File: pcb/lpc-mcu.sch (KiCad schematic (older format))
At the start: 1 part

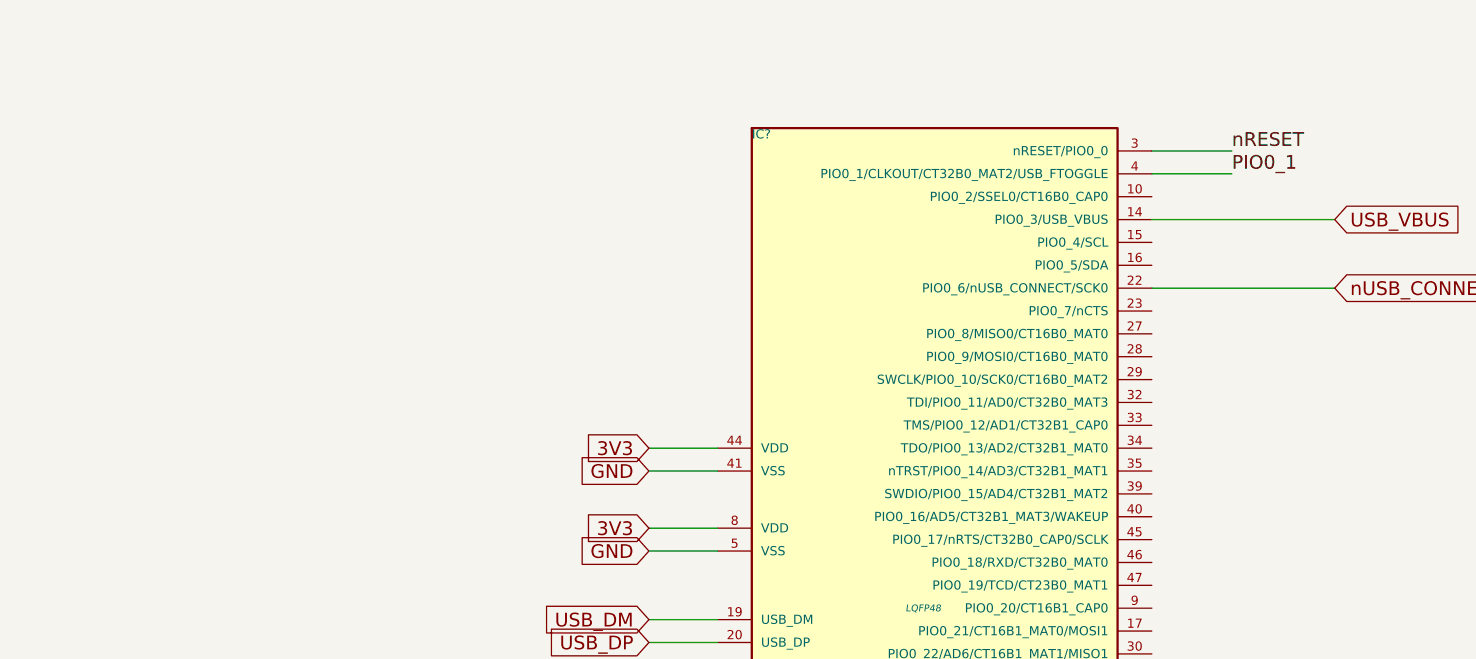
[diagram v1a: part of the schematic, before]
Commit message: added SWD connector
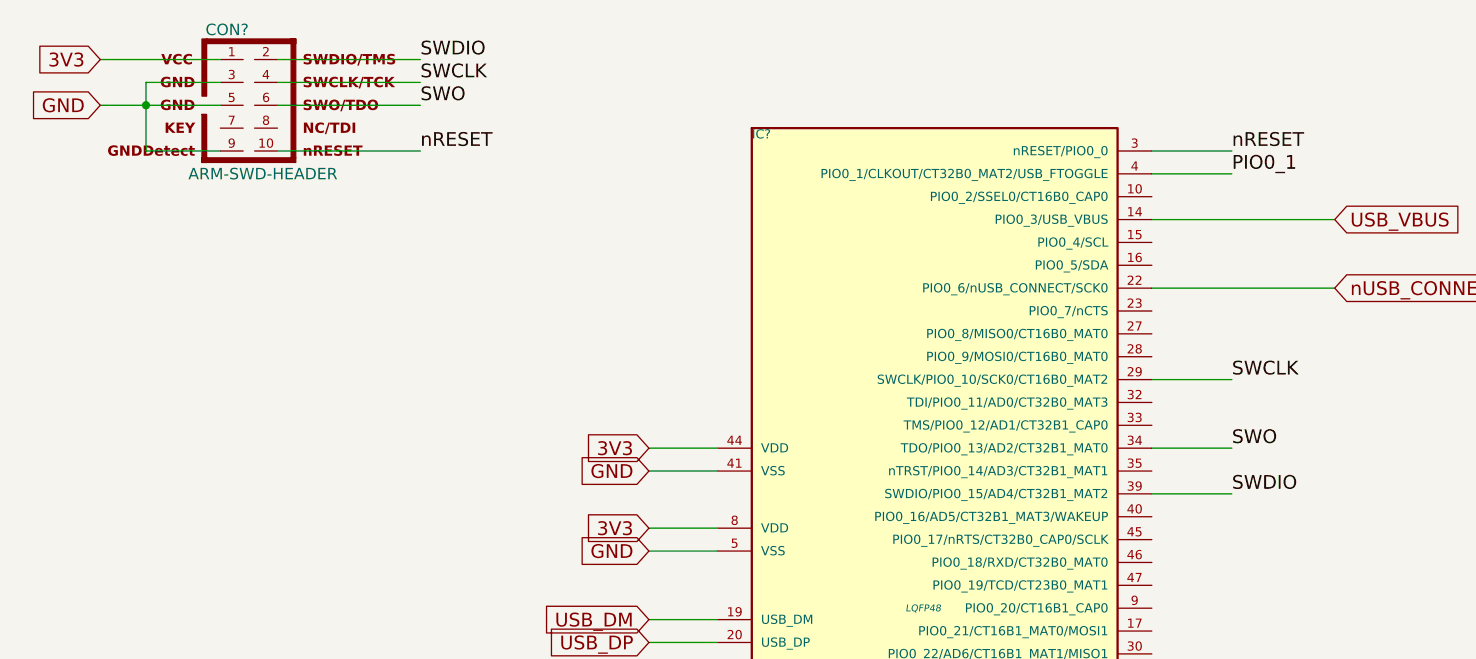
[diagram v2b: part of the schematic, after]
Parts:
- added CON?: ARM-SWD-HEADER, pin_array_5x2_50mil_smd, symbol ARM-SWD-HEADER
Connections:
- net 3V3: now also CON?.1
- net GND: now also CON?.3, CON?.5, CON?.9
- net nRESET: now also CON?.10
- net SWCLK: now reaches IC?.29 (SWCLK/PIO0_10/SCK0/CT16B0_MAT2)
- net SWCLK: now also CON?.4
- net SWO: now reaches IC?.34 (TDO/PIO0_13/AD2/CT32B1_MAT0)
- net SWO: now also CON?.6
- net SWDIO: now reaches IC?.39 (SWDIO/PIO0_15/AD4/CT32B1_MAT2)
- net SWDIO: now also CON?.2
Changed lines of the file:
@@
 Wire Wire Line
 	4350 4350 4050 4350
+$Comp
+L ARM-SWD-HEADER CON?
+U 1 1 549D5A39
+P 2300 2000
+F 0 "CON?" H 2205 2330 50  0000 C CNN
+F 1 "ARM-SWD-HEADER" H 2035 1670 50  0000 L BNN
+F 2 "pin_array_5x2_50mil_smd" V 1875 2000 50  0001 C CNN
+F 3 "~" H 2375 2000 60  0000 C CNN
+	1    2300 2000
+	1    0    0    -1
+$EndComp
+Text GLabel 1650 1800 0    60   Input ~ 0
+3V3
+Text GLabel 1650 2000 0    60   Input ~ 0
+GND
+Text Label 3050 1800 0    60   ~ 0
+SWDIO
+Text Label 3050 1900 0    60   ~ 0
+SWCLK
+Text Label 3050 2200 0    60   ~ 0
+nRESET
+Wire Wire Line
+	3050 2200 2425 2200
+Wire Wire Line
+	2425 1900 3050 1900
+Wire Wire Line
+	3050 1800 2425 1800
+Wire Wire Line
+	2175 1800 1650 1800
+Wire Wire Line
+	1650 2000 2175 2000
+Wire Wire Line
+	2175 1900 1850 1900
+Wire Wire Line
+	1850 1900 1850 2200
+Connection ~ 1850 2000
+Wire Wire Line
+	1850 2200 2175 2200
+Text Label 6600 3200 0    60   ~ 0
+SWCLK
+Text Label 6600 3700 0    60   ~ 0
+SWDIO
+Wire Wire Line
+	6600 3700 6250 3700
+Wire Wire Line
+	6250 3200 6600 3200
+Text Label 3050 2000 0    60   ~ 0
+SWO
+Text Label 6600 3500 0    60   ~ 0
+SWO
+Wire Wire Line
+	6600 3500 6250 3500
+Wire Wire Line
+	3050 2000 2425 2000
 $EndSCHEMATC

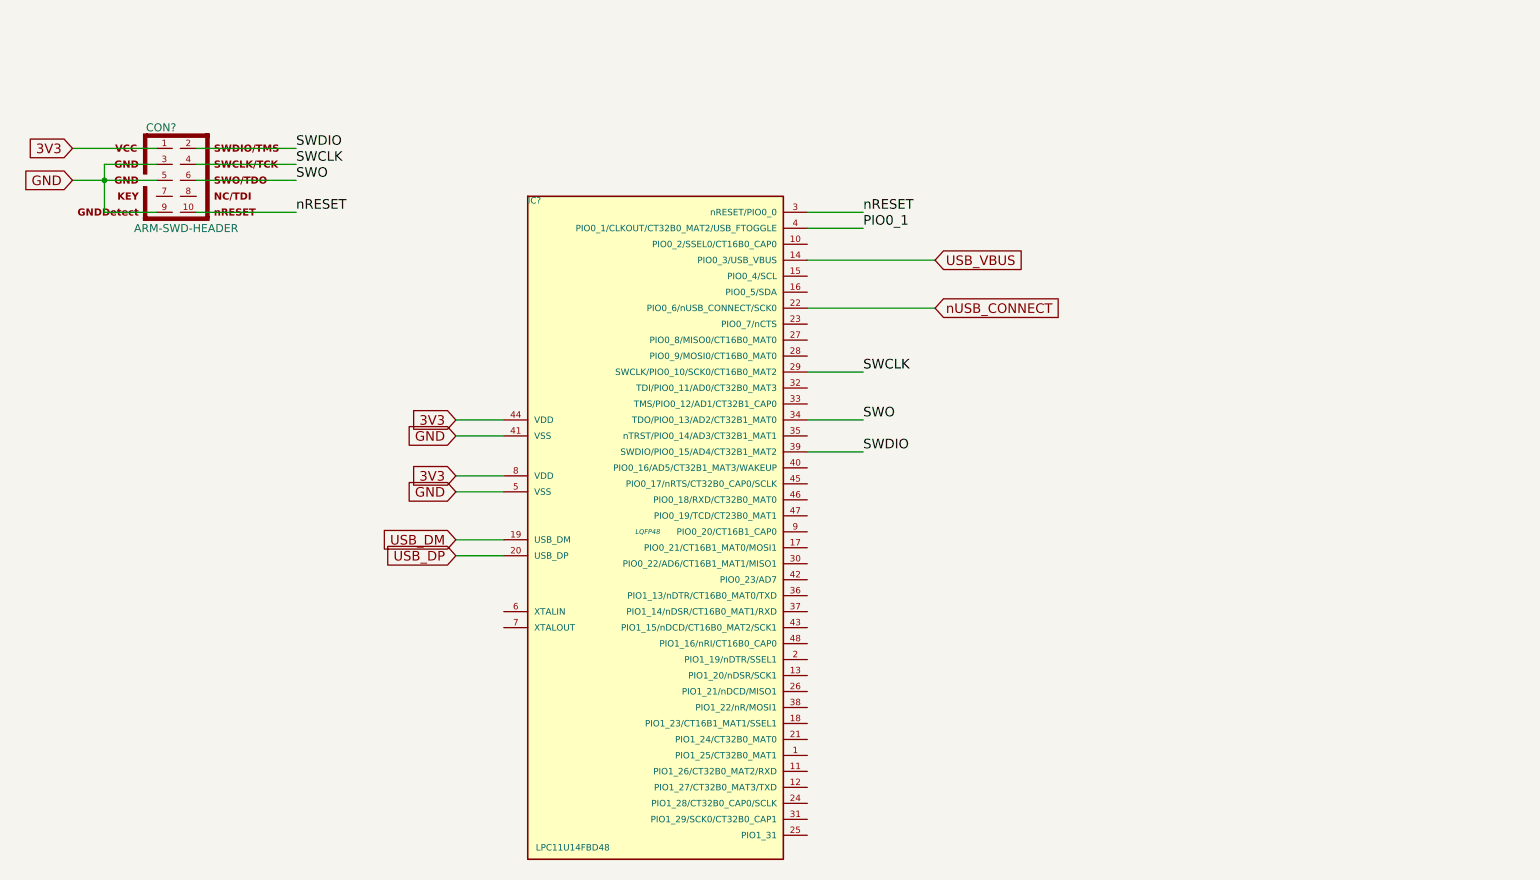
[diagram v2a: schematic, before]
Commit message: added reset pullup, some caps, usb resistors, explanation for nUSB_CONNECT
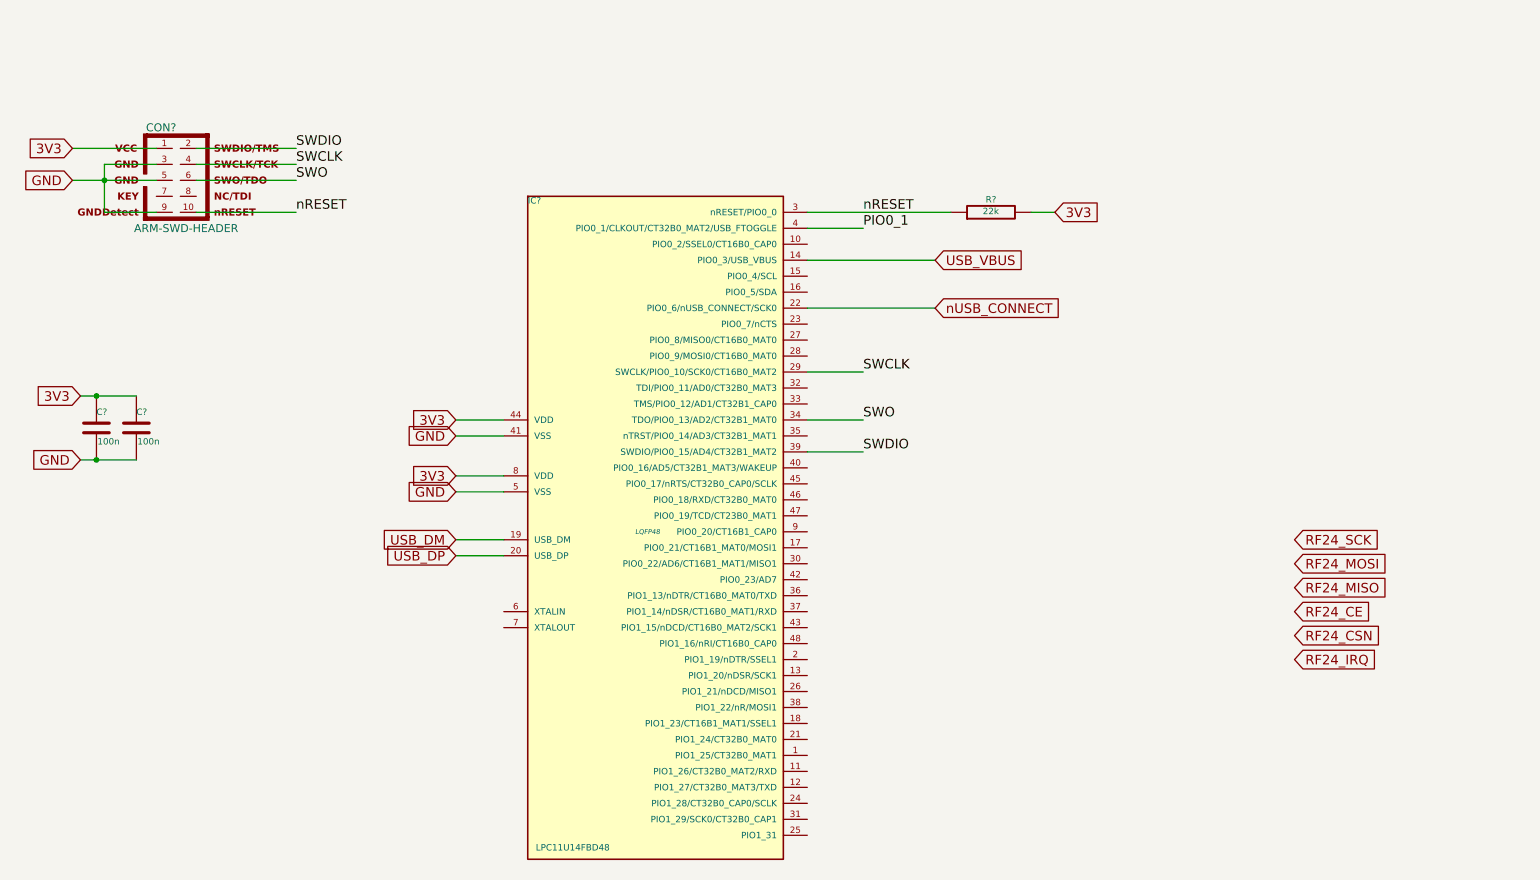
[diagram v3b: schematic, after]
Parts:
- added C? (x2): 100n, ~, symbol C
- added R?: 22k, ~, symbol R
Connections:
- net 3V3: now also C?.1, C?.1, R?.2
- net GND: now also C?.2, C?.2
- net nRESET: now also R?.1
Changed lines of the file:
@@
 	6600 2300 6250 2300
-Wire Wire Line
-	6250 2200 6600 2200
 Wire Wire Line
 	7050 2500 6250 2500
@@
 Wire Wire Line
 	3050 2000 2425 2000
+Text GLabel 9300 4250 2    60   Input ~ 0
+RF24_SCK
+Text GLabel 9300 4400 2    60   Input ~ 0
+RF24_MOSI
+Text GLabel 9300 4550 2    60   Input ~ 0
+RF24_MISO
+Text GLabel 9300 4700 2    60   Input ~ 0
+RF24_CE
+Text GLabel 9300 4850 2    60   Input ~ 0
+RF24_CSN
+Text GLabel 9300 5000 2    60   Input ~ 0
+RF24_IRQ
+$Comp
+L C C?
+U 1 1 549D5E39
+P 1800 3550
+F 0 "C?" H 1800 3650 40  0000 L CNN
+F 1 "100n" H 1806 3465 40  0000 L CNN
+F 2 "~" H 1838 3400 30  0000 C CNN
+F 3 "~" H 1800 3550 60  0000 C CNN
+	1    1800 3550
+	1    0    0    -1
+$EndComp
+$Comp
+L C C?
+U 1 1 549D5E52
+P 2050 3550
+F 0 "C?" H 2050 3650 40  0000 L CNN
+F 1 "100n" H 2056 3465 40  0000 L CNN
+F 2 "~" H 2088 3400 30  0000 C CNN
+F 3 "~" H 2050 3550 60  0000 C CNN
+	1    2050 3550
+	1    0    0    -1
+$EndComp
+Wire Wire Line
+	1700 3350 2050 3350
+Wire Wire Line
+	1700 3750 2050 3750
+Text GLabel 1700 3350 0    60   Input ~ 0
+3V3
+Text GLabel 1700 3750 0    60   Input ~ 0
+GND
+Connection ~ 1800 3750
+Connection ~ 1800 3350
+$Comp
+L R R?
+U 1 1 549D5EC0
+P 7400 2200
+F 0 "R?" V 7480 2200 40  0000 C CNN
+F 1 "22k" V 7407 2201 40  0000 C CNN
+F 2 "~" V 7330 2200 30  0000 C CNN
+F 3 "~" H 7400 2200 30  0000 C CNN
+	1    7400 2200
+	0    -1   -1   0
+$EndComp
+Text GLabel 7800 2200 2    60   Input ~ 0
+3V3
+Wire Wire Line
+	6250 2200 7150 2200
+Wire Wire Line
+	7650 2200 7800 2200
 $EndSCHEMATC

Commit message: thought through power situation a bit more, added some TO DO messages
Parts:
- added R?: NC, ~, symbol R
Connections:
- net 3V3: now also R?.1; no longer CON?.1
- new net: CON?.1, R?.2
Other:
- note added: "Debugger not connected to 3V3 by\ndefault, to avoid accidentally\nbackfeeding power into the regulator."
- note added: "One bypass cap for each VDD/VSS pair."
- note added: "TO DO: figure out if we need to reduce the USB\nbus voltage before it gets to the MCU."
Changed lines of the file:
@@
 	1    0    0    -1
 $EndComp
-Text GLabel 1650 1800 0    60   Input ~ 0
+Text GLabel 1650 1200 0    60   Input ~ 0
 3V3
 Text GLabel 1650 2000 0    60   Input ~ 0
@@
 Wire Wire Line
 	3050 1800 2425 1800
-Wire Wire Line
-	2175 1800 1650 1800
 Wire Wire Line
 	1650 2000 2175 2000
@@
 Wire Wire Line
 	7650 2200 7800 2200
+$Comp
+L R R?
+U 1 1 549D6951
+P 1700 1500
+F 0 "R?" V 1780 1500 40  0000 C CNN
+F 1 "NC" V 1707 1501 40  0000 C CNN
+F 2 "~" V 1630 1500 30  0000 C CNN
+F 3 "~" H 1700 1500 30  0000 C CNN
+	1    1700 1500
+	1    0    0    -1
+$EndComp
+Wire Wire Line
+	2175 1800 1700 1800
+Wire Wire Line
+	1700 1800 1700 1750
+Wire Wire Line
+	1700 1250 1700 1200
+Wire Wire Line
+	1700 1200 1650 1200
+Text Notes 1825 1250 0    60   ~ 0
+Debugger not connected to 3V3 by\ndefault, to avoid accidentally\nbackfeeding power into the regulator.
+Text Notes 1275 3200 0    60   ~ 0
+One bypass cap for each VDD/VSS pair.
+Text Notes 7675 2500 0    60   ~ 0
+TO DO: figure out if we need to reduce the USB\nbus voltage before it gets to the MCU.
 $EndSCHEMATC

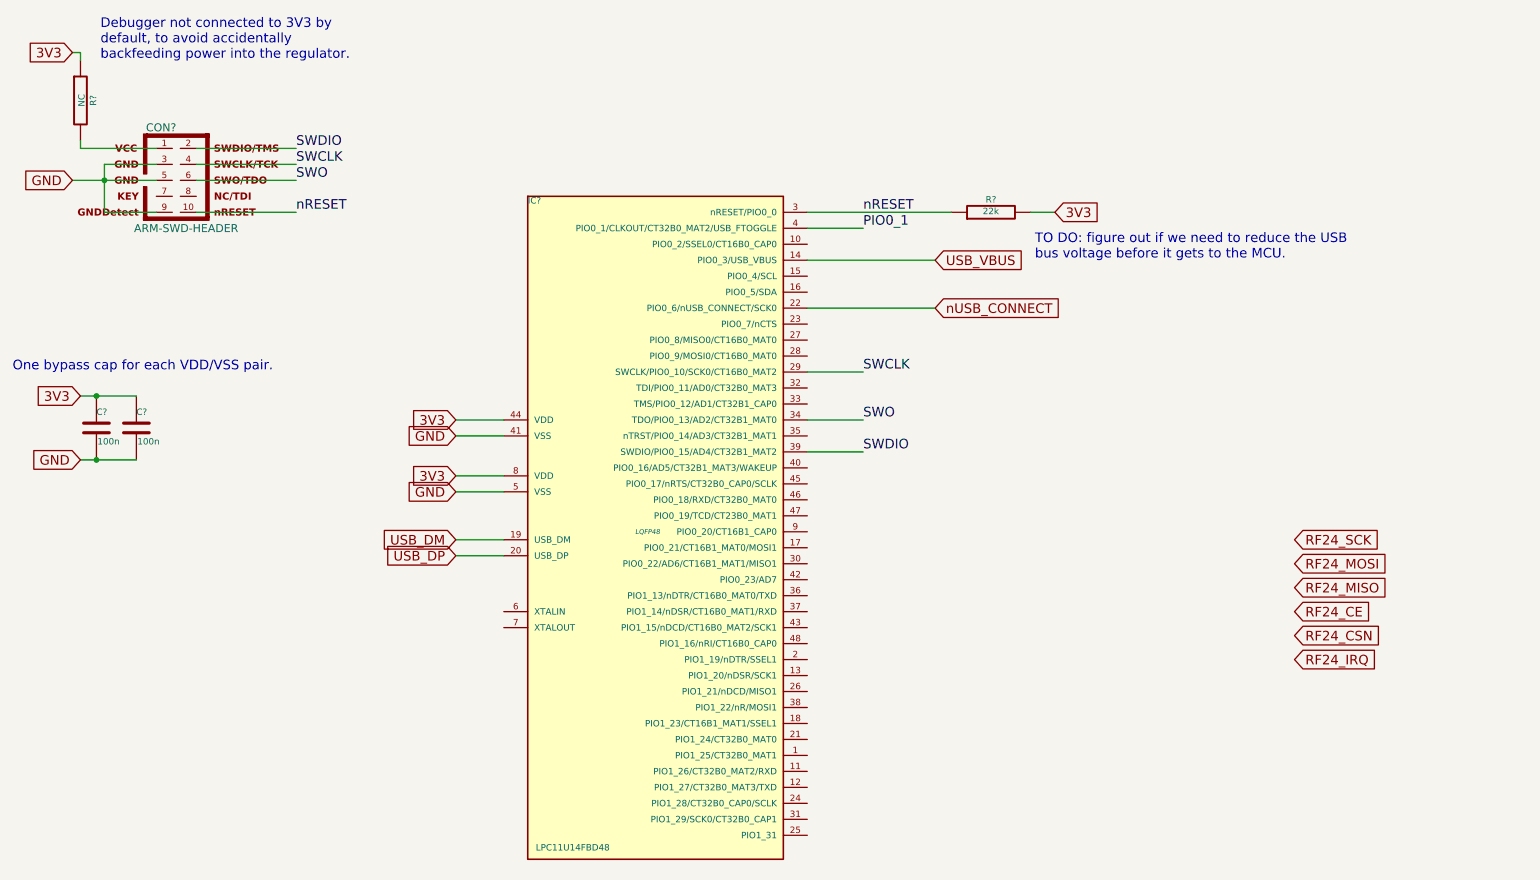
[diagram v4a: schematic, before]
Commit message: made a usb-a plug from usb-if and wikipedia docs
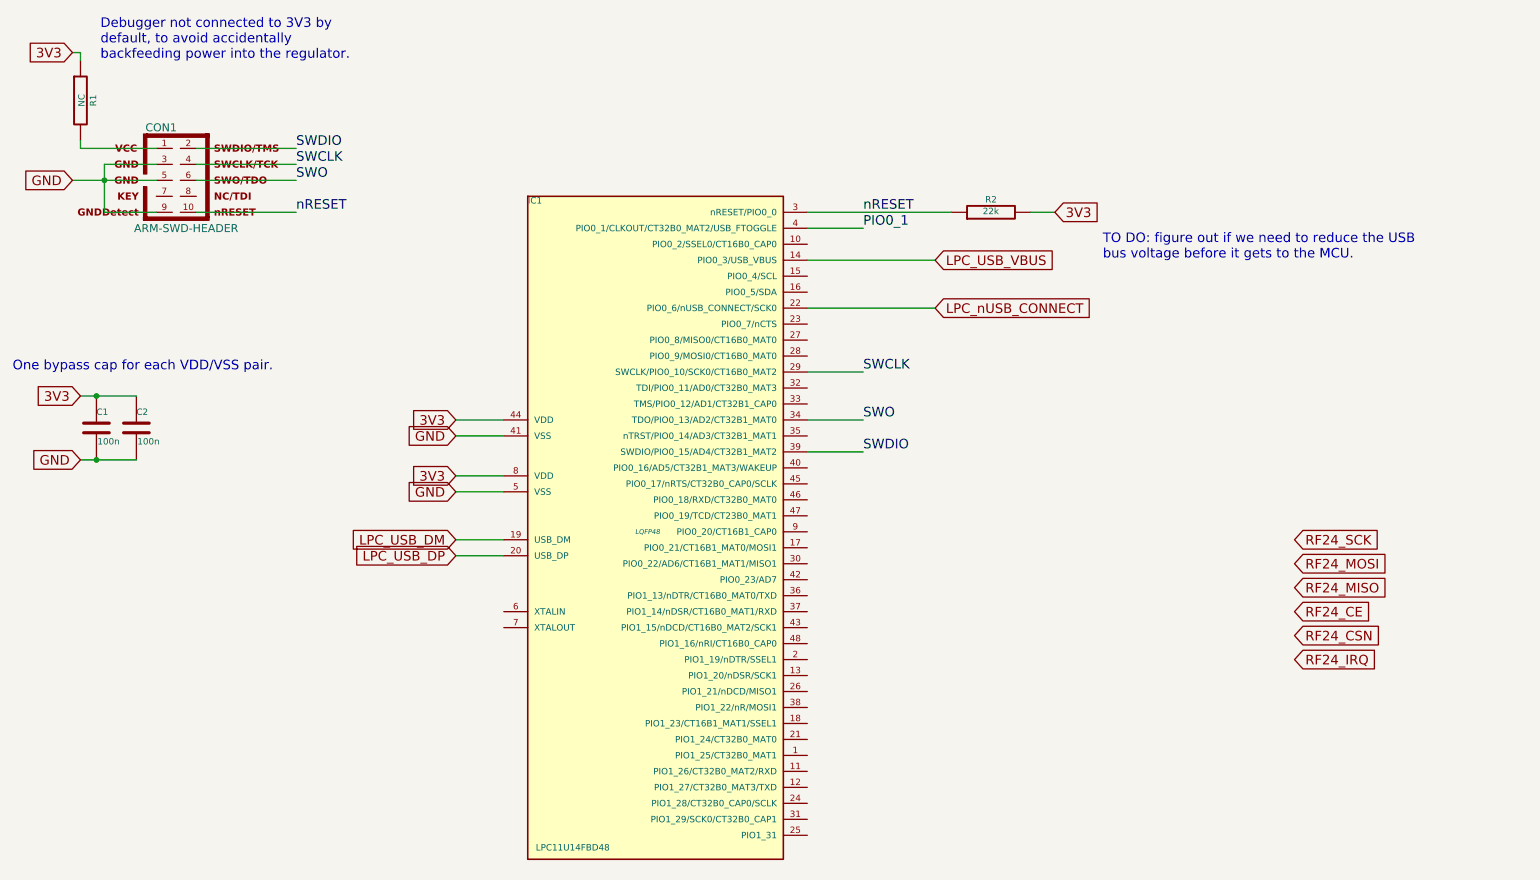
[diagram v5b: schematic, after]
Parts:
- gave numbers to parts that had none: 6
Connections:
- net USB_DM renamed LPC_USB_DM
- net USB_DP renamed LPC_USB_DP
- net USB_VBUS renamed LPC_USB_VBUS
- net nUSB_CONNECT renamed LPC_nUSB_CONNECT
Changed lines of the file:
@@
 $EndDescr
 $Comp
-L LPC11U14FBD48 IC?
+L LPC11U14FBD48 IC1
 U 1 1 549D53F4
 P 5250 4200
-F 0 "IC?" H 4500 6250 40  0000 L BNN
+F 0 "IC1" H 4500 6250 40  0000 L BNN
 F 1 "LPC11U14FBD48" H 4550 2200 40  0000 L BNN
 F 2 "LQFP48" H 5250 4200 30  0000 C CIN
@@
 GND
 Text GLabel 4050 4250 0    60   Input ~ 0
-USB_DM
+LPC_USB_DM
 Text GLabel 4050 4350 0    60   Input ~ 0
-USB_DP
+LPC_USB_DP
 Text Label 6600 2200 0    60   ~ 0
 nRESET
 Text GLabel 7050 2500 2    60   Input ~ 0
-USB_VBUS
+LPC_USB_VBUS
 Text Label 6600 2300 0    60   ~ 0
 PIO0_1
@@
 	7050 2500 6250 2500
 Text GLabel 7050 2800 2    60   Input ~ 0
-nUSB_CONNECT
+LPC_nUSB_CONNECT
 Wire Wire Line
 	7050 2800 6250 2800
@@
 	4350 4350 4050 4350
 $Comp
-L ARM-SWD-HEADER CON?
+L ARM-SWD-HEADER CON1
 U 1 1 549D5A39
 P 2300 2000
-F 0 "CON?" H 2205 2330 50  0000 C CNN
+F 0 "CON1" H 2205 2330 50  0000 C CNN
 F 1 "ARM-SWD-HEADER" H 2035 1670 50  0000 L BNN
 F 2 "pin_array_5x2_50mil_smd" V 1875 2000 50  0001 C CNN
@@
 RF24_IRQ
 $Comp
-L C C?
+L C C1
 U 1 1 549D5E39
 P 1800 3550
-F 0 "C?" H 1800 3650 40  0000 L CNN
+F 0 "C1" H 1800 3650 40  0000 L CNN
 F 1 "100n" H 1806 3465 40  0000 L CNN
 F 2 "~" H 1838 3400 30  0000 C CNN
@@
 $EndComp
 $Comp
-L C C?
+L C C2
 U 1 1 549D5E52
 P 2050 3550
-F 0 "C?" H 2050 3650 40  0000 L CNN
+F 0 "C2" H 2050 3650 40  0000 L CNN
 F 1 "100n" H 2056 3465 40  0000 L CNN
 F 2 "~" H 2088 3400 30  0000 C CNN
@@
 Connection ~ 1800 3350
 $Comp
-L R R?
+L R R2
 U 1 1 549D5EC0
 P 7400 2200
-F 0 "R?" V 7480 2200 40  0000 C CNN
+F 0 "R2" V 7480 2200 40  0000 C CNN
 F 1 "22k" V 7407 2201 40  0000 C CNN
 F 2 "~" V 7330 2200 30  0000 C CNN
@@
 	7650 2200 7800 2200
 $Comp
-L R R?
+L R R1
 U 1 1 549D6951
 P 1700 1500
-F 0 "R?" V 1780 1500 40  0000 C CNN
+F 0 "R1" V 1780 1500 40  0000 C CNN
 F 1 "NC" V 1707 1501 40  0000 C CNN
 F 2 "~" V 1630 1500 30  0000 C CNN
@@
 Text Notes 1275 3200 0    60   ~ 0
 One bypass cap for each VDD/VSS pair.
-Text Notes 7675 2500 0    60   ~ 0
+Text Notes 8100 2500 0    60   ~ 0
 TO DO: figure out if we need to reduce the USB\nbus voltage before it gets to the MCU.
 $EndSCHEMATC
